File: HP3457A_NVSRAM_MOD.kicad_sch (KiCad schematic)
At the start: 18 parts, among them J1 Conn_01x02, U1 TL431DBZ, U10 TC5564APL_Adapter, U2 74AHC2G00, U3 STK12C68

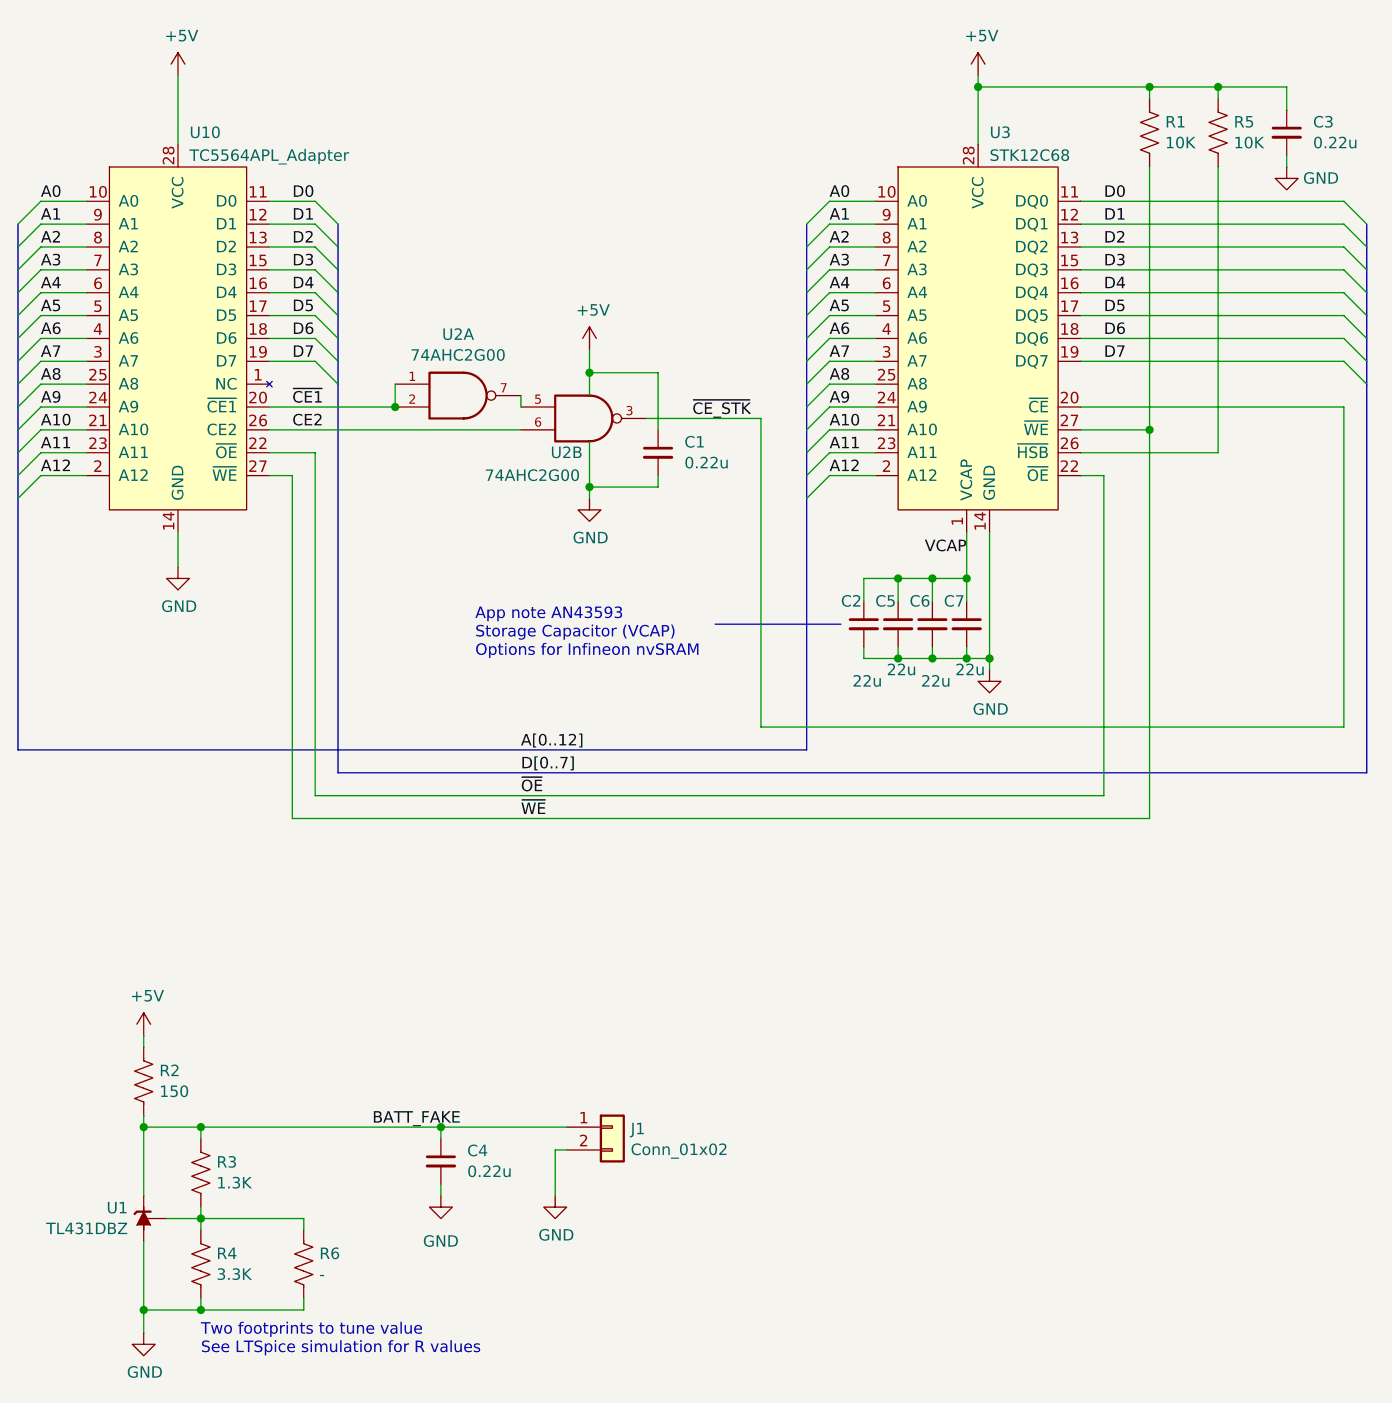
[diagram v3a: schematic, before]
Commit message: Improved labelling and checked board in new KiCad version.
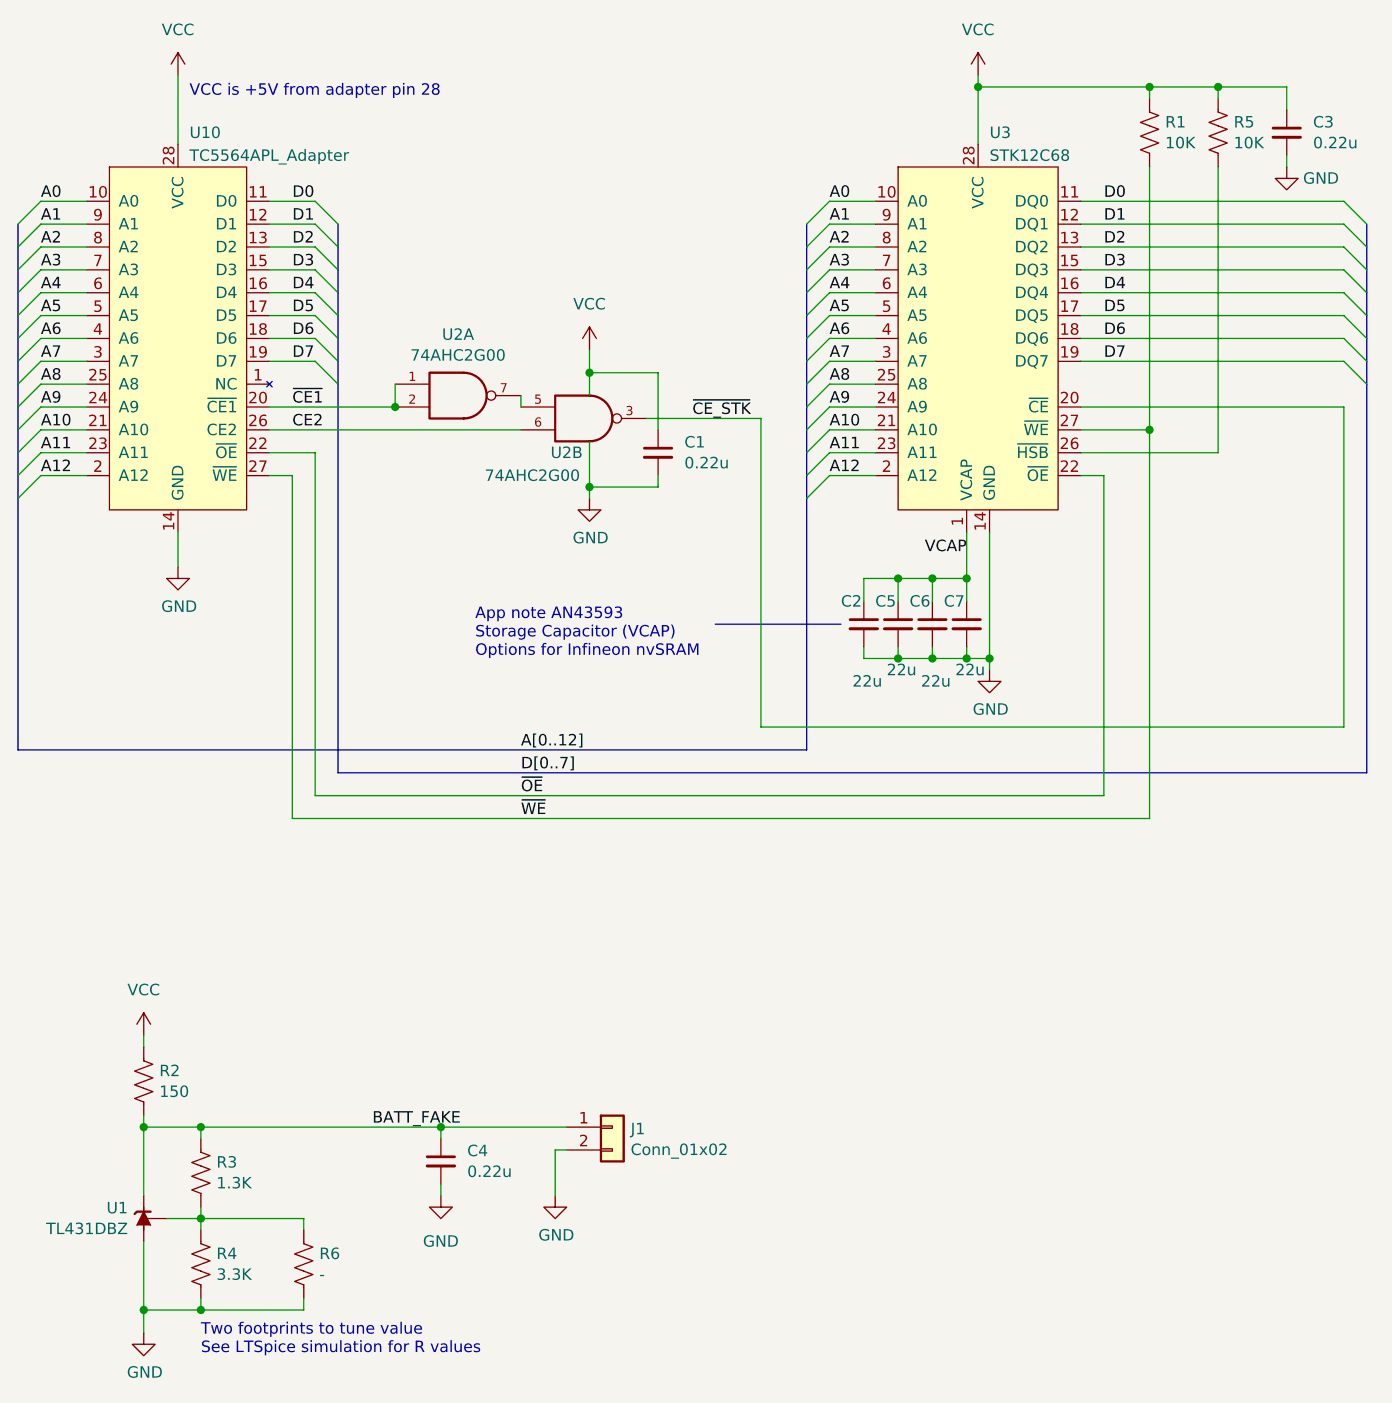
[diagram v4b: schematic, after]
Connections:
- net +5V renamed VCC
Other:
- note added: "VCC is +5V from adapter pin 28"
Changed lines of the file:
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@@
+    (stroke (width 0) (type default) (color 0 0 0 0))
+  )
+  (wire (pts (xy 66.04 38.1) (xy 66.04 45.72))
     (stroke (width 0) (type default) (color 0 0 0 0))
   )
@@
     (stroke (width 0) (type default) (color 0 0 0 0))
   )
-  (wire (pts (xy 66.04 45.72) (xy 66.04 38.1))
-    (stroke (width 0) (type default) (color 0 0 0 0))
-  )
   (wire (pts (xy 156.21 88.9) (xy 156.21 102.87))
     (stroke (width 0) (type default) (color 0 0 0 0))
@@
   (wire (pts (xy 143.51 57.15) (xy 138.43 57.15))
     (stroke (width 0) (type default) (color 0 0 0 0))
+  )
+  (text "VCC is +5V from adapter pin 28" (at 67.31 40.64 0)
+    (effects (font (size 1.27 1.27)) (justify left bottom))
   )
   (text "Two footprints to tune value\nSee LTSpice simulation for R values"
@@
     (pin "1")
   )
-  (symbol (lib_id "power:+5V") (at 62.23 144.78 0) (unit 1)
-    (in_bom yes) (on_board yes)
-    (property "Reference" "#PWR0108" (id 0) (at 62.23 148.59 0)
-      (effects (font (size 1.27 1.27)) hide)
-    )
-    (property "Value" "+5V" (id 1) (at 62.611 140.3858 0))
-    (property "Footprint" "" (id 2) (at 62.23 144.78 0)
-      (effects (font (size 1.27 1.27)) hide)
-    )
-    (property "Datasheet" "" (id 3) (at 62.23 144.78 0)
-      (effects (font (size 1.27 1.27)) hide)
-    )
-    (pin "1")
-  )
   (symbol (lib_id "74xGxx:74AHC2G00") (at 97.79 73.66 0) (unit 1)
     (in_bom yes) (on_board yes)
@@
     (pin "1")
   )
-  (symbol (lib_id "power:+5V") (at 111.76 68.58 0) (unit 1)
-    (in_bom yes) (on_board yes)
-    (property "Reference" "#PWR0104" (id 0) (at 111.76 72.39 0)
-      (effects (font (size 1.27 1.27)) hide)
-    )
-    (property "Value" "+5V" (id 1) (at 112.141 64.1858 0))
-    (property "Footprint" "" (id 2) (at 111.76 68.58 0)
-      (effects (font (size 1.27 1.27)) hide)
-    )
-    (property "Datasheet" "" (id 3) (at 111.76 68.58 0)
-      (effects (font (size 1.27 1.27)) hide)
-    )
-    (pin "1")
-  )
-  (symbol (lib_id "power:+5V") (at 66.04 38.1 0) (unit 1)
-    (in_bom yes) (on_board yes)
-    (property "Reference" "#PWR0105" (id 0) (at 66.04 41.91 0)
-      (effects (font (size 1.27 1.27)) hide)
-    )
-    (property "Value" "+5V" (id 1) (at 66.421 33.7058 0))
-    (property "Footprint" "" (id 2) (at 66.04 38.1 0)
-      (effects (font (size 1.27 1.27)) hide)
-    )
-    (property "Datasheet" "" (id 3) (at 66.04 38.1 0)
-      (effects (font (size 1.27 1.27)) hide)
-    )
-    (pin "1")
-  )
-  (symbol (lib_id "power:+5V") (at 154.94 38.1 0) (unit 1)
-    (in_bom yes) (on_board yes)
-    (property "Reference" "#PWR0106" (id 0) (at 154.94 41.91 0)
-      (effects (font (size 1.27 1.27)) hide)
-    )
-    (property "Value" "+5V" (id 1) (at 155.321 33.7058 0))
-    (property "Footprint" "" (id 2) (at 154.94 38.1 0)
-      (effects (font (size 1.27 1.27)) hide)
-    )
-    (property "Datasheet" "" (id 3) (at 154.94 38.1 0)
-      (effects (font (size 1.27 1.27)) hide)
-    )
-    (pin "1")
-  )
   (symbol (lib_id "Device:C_Small") (at 119.38 80.01 0) (unit 1)
     (in_bom yes) (on_board yes)
@@
     (pin "1")
   )
+  (symbol (lib_id "power:VCC") (at 111.76 68.58 0) (unit 1)
+    (in_bom yes) (on_board yes) (fields_autoplaced)
+    (property "Reference" "#PWR0104" (id 0) (at 111.76 72.39 0)
+      (effects (font (size 1.27 1.27)) hide)
+    )
+    (property "Value" "VCC" (id 1) (at 111.76 63.5 0))
+    (property "Footprint" "" (id 2) (at 111.76 68.58 0)
+      (effects (font (size 1.27 1.27)) hide)
+    )
+    (property "Datasheet" "" (id 3) (at 111.76 68.58 0)
+      (effects (font (size 1.27 1.27)) hide)
+    )
+    (pin "1")
+  )
   (symbol (lib_id "Device:C_Small") (at 95.25 158.75 0) (unit 1)
     (in_bom yes) (on_board yes)
@@
     (pin "1")
     (pin "2")
+  )
+  (symbol (lib_id "power:VCC") (at 62.23 144.78 0) (unit 1)
+    (in_bom yes) (on_board yes) (fields_autoplaced)
+    (property "Reference" "#PWR0108" (id 0) (at 62.23 148.59 0)
+      (effects (font (size 1.27 1.27)) hide)
+    )
+    (property "Value" "VCC" (id 1) (at 62.23 139.7 0))
+    (property "Footprint" "" (id 2) (at 62.23 144.78 0)
+      (effects (font (size 1.27 1.27)) hide)
+    )
+    (property "Datasheet" "" (id 3) (at 62.23 144.78 0)
+      (effects (font (size 1.27 1.27)) hide)
+    )
+    (pin "1")
+  )
+  (symbol (lib_id "power:VCC") (at 66.04 38.1 0) (unit 1)
+    (in_bom yes) (on_board yes) (fields_autoplaced)
+    (property "Reference" "#PWR0106" (id 0) (at 66.04 41.91 0)
+      (effects (font (size 1.27 1.27)) hide)
+    )
+    (property "Value" "VCC" (id 1) (at 66.04 33.02 0))
+    (property "Footprint" "" (id 2) (at 66.04 38.1 0)
+      (effects (font (size 1.27 1.27)) hide)
+    )
+    (property "Datasheet" "" (id 3) (at 66.04 38.1 0)
+      (effects (font (size 1.27 1.27)) hide)
+    )
+    (pin "1")
   )
   (symbol (lib_id "Device:C_Small") (at 149.86 99.06 0) (unit 1)
@@
     (pin "1")
     (pin "2")
+  )
+  (symbol (lib_id "power:VCC") (at 154.94 38.1 0) (unit 1)
+    (in_bom yes) (on_board yes) (fields_autoplaced)
+    (property "Reference" "#PWR0105" (id 0) (at 154.94 41.91 0)
+      (effects (font (size 1.27 1.27)) hide)
+    )
+    (property "Value" "VCC" (id 1) (at 154.94 33.02 0))
+    (property "Footprint" "" (id 2) (at 154.94 38.1 0)
+      (effects (font (size 1.27 1.27)) hide)
+    )
+    (property "Datasheet" "" (id 3) (at 154.94 38.1 0)
+      (effects (font (size 1.27 1.27)) hide)
+    )
+    (pin "1")
   )
   (sheet_instances
@@
       (reference "#PWR0103") (unit 1) (value "GND") (footprint "")
     )
-    (path "/00000000-0000-0000-0000-0000634e78d2"
-      (reference "#PWR0104") (unit 1) (value "+5V") (footprint "")
-    )
-    (path "/00000000-0000-0000-0000-0000634e7f0f"
-      (reference "#PWR0105") (unit 1) (value "+5V") (footprint "")
-    )
-    (path "/00000000-0000-0000-0000-0000634e86dd"
-      (reference "#PWR0106") (unit 1) (value "+5V") (footprint "")
+    (path "/2f119086-82af-49ab-ae59-4079739fa2a8"
+      (reference "#PWR0104") (unit 1) (value "VCC") (footprint "")
+    )
+    (path "/f4e6f87d-2e36-4343-816d-efee79e6b09a"
+      (reference "#PWR0105") (unit 1) (value "VCC") (footprint "")
+    )
+    (path "/6f23b1db-e358-4c6f-b9de-28978efc39fe"
+      (reference "#PWR0106") (unit 1) (value "VCC") (footprint "")
     )
     (path "/00000000-0000-0000-0000-00006345e384"
       (reference "#PWR0107") (unit 1) (value "GND") (footprint "")
     )
-    (path "/00000000-0000-0000-0000-00006345e8f9"
-      (reference "#PWR0108") (unit 1) (value "+5V") (footprint "")
+    (path "/6f13155a-20d7-43da-953e-8018144bc59a"
+      (reference "#PWR0108") (unit 1) (value "VCC") (footprint "")
     )
     (path "/00000000-0000-0000-0000-00006349c9d2"
